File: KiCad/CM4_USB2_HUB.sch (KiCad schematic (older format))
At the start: 31 parts, among them IC1 USB2517-JZX, J10 72309-8014BLF, J11 10104110-0001LF, J12 SS-52100-002, J4 72309-8014BLF, J9 Conn_02x05_Odd_Even, U3 FSUSB42MUX, Y1 24MHz

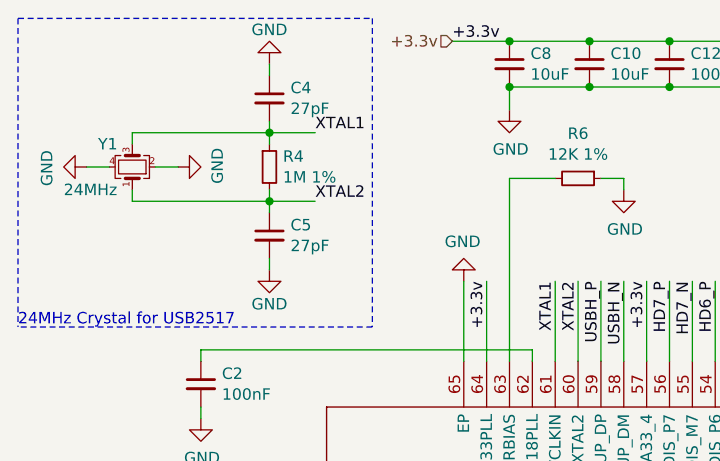
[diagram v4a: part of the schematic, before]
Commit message: Updated Y1 capacitors
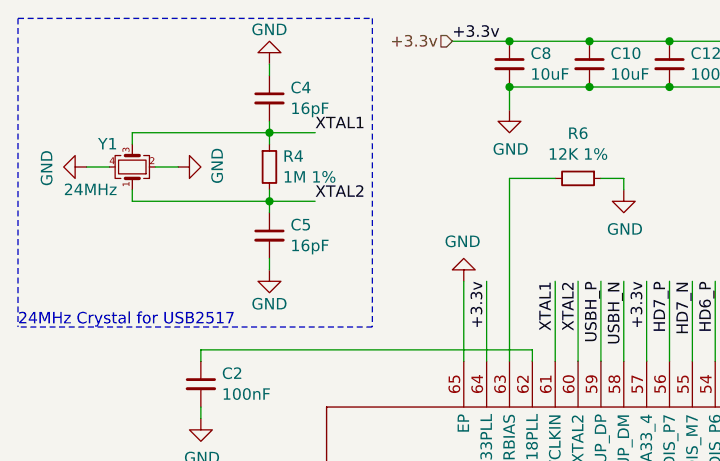
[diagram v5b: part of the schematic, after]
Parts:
- C4, C5: value 27pF -> 16pF; footprint (none) -> CM4_MATX:C_0402_1005Metric_Pad0.74x0.62mm_HandSolder; Description Load Capacitors for Y1 Crystal -> 10V 16pF X8R 0402 5% Tol; Mfr. (none) -> KEMET; Mfr. No (none) -> C0402C160J8HACTU; Mouser Part Number (none) -> 80-C0402C160J8HACTU; Mouser Price/Stock (none) -> https://www.mouser.co.uk/ProductDetail/KEMET/C0402C160J8HAC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
- R12: footprint (none) -> CM4_MATX:R_0603_1608Metric_Pad0.98x0.95mm_HandSolder
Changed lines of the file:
@@
 F 0 "R12" H 7850 6050 50  0000 L CNN
 F 1 "2.2K 1%" H 7700 5950 50  0000 L CNN
-F 2 "" H 8050 6000 50  0001 C CNN
+F 2 "CM4_MATX:R_0603_1608Metric_Pad0.98x0.95mm_HandSolder" H 8050 6000 50  0001 C CNN
 F 3 "~" H 8050 6000 50  0001 C CNN
 	1    8050 6000
@@
 P 1600 1450
 F 0 "C5" H 1692 1496 50  0000 L CNN
-F 1 "27pF" H 1692 1405 50  0000 L CNN
-F 2 "" H 1600 1450 50  0001 C CNN
-F 3 "~" H 1600 1450 50  0001 C CNN
-F 4 "Load Capacitors for Y1 Crystal" H 1600 1450 50  0001 C CNN "Description"
+F 1 "16pF" H 1692 1405 50  0000 L CNN
+F 2 "CM4_MATX:C_0402_1005Metric_Pad0.74x0.62mm_HandSolder" H 1600 1450 50  0001 C CNN
+F 3 "https://www.mouser.co.uk/datasheet/2/212/KEM_C1007_X8R_ULTRA_150C_SMD-1102703.pdf" H 1600 1450 50  0001 C CNN
+F 4 "10V 16pF X8R 0402 5% Tol" H 1600 1450 50  0001 C CNN "Description"
+F 5 "KEMET" H 1600 1450 50  0001 C CNN "Mfr."
+F 6 "C0402C160J8HACTU" H 1600 1450 50  0001 C CNN "Mfr. No"
+F 7 "80-C0402C160J8HACTU" H 1600 1450 50  0001 C CNN "Mouser Part Number"
+F 8 "https://www.mouser.co.uk/ProductDetail/KEMET/C0402C160J8HACTU/?qs=sGAEpiMZZMvsSlwiRhF8qtsBU8Zhqm2Rf2RCdR0OYjobkxwyt1Kljg%3D%3D" H 1600 1450 50  0001 C CNN "Mouser Price/Stock"
 	1    1600 1450
 	1    0    0    -1
@@
 P 1600 850
 F 0 "C4" H 1692 896 50  0000 L CNN
-F 1 "27pF" H 1692 805 50  0000 L CNN
-F 2 "" H 1600 850 50  0001 C CNN
-F 3 "~" H 1600 850 50  0001 C CNN
-F 4 "Load Capacitors for Y1 Crystal" H 1600 850 50  0001 C CNN "Description"
+F 1 "16pF" H 1692 805 50  0000 L CNN
+F 2 "CM4_MATX:C_0402_1005Metric_Pad0.74x0.62mm_HandSolder" H 1600 850 50  0001 C CNN
+F 3 "https://www.mouser.co.uk/datasheet/2/212/KEM_C1007_X8R_ULTRA_150C_SMD-1102703.pdf" H 1600 850 50  0001 C CNN
+F 4 "10V 16pF X8R 0402 5% Tol" H 1600 850 50  0001 C CNN "Description"
+F 5 "KEMET" H 1600 850 50  0001 C CNN "Mfr."
+F 6 "C0402C160J8HACTU" H 1600 850 50  0001 C CNN "Mfr. No"
+F 7 "80-C0402C160J8HACTU" H 1600 850 50  0001 C CNN "Mouser Part Number"
+F 8 "https://www.mouser.co.uk/ProductDetail/KEMET/C0402C160J8HACTU/?qs=sGAEpiMZZMvsSlwiRhF8qtsBU8Zhqm2Rf2RCdR0OYjobkxwyt1Kljg%3D%3D" H 1600 850 50  0001 C CNN "Mouser Price/Stock"
 	1    1600 850
 	1    0    0    -1

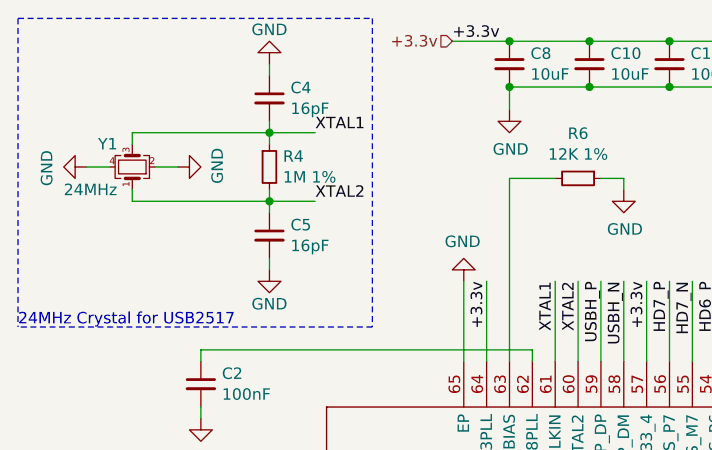
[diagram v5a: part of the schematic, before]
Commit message: Removed R4
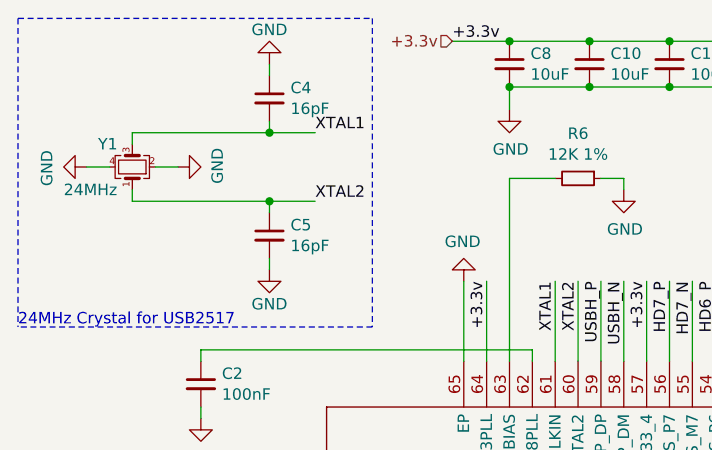
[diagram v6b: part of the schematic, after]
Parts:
- removed R4: 1M 1%, symbol CM4_MATX:R_Small
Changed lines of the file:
@@
 Wire Wire Line
 	1600 1000 1000 1000
-Wire Wire Line
-	1600 1300 1600 1250
 Connection ~ 1600 1300
 Wire Wire Line
@@
 Wire Wire Line
 	1600 1000 1800 1000
-Wire Wire Line
-	1600 1050 1600 1000
 $Comp
 L CM4_MATX:C_Small C5
@@
 Text Label 1800 1000 0    50   ~ 0
 XTAL1
-$Comp
-L CM4_MATX:R_Small R4
-U 1 1 5FE3FBDB
-P 1600 1150
-F 0 "R4" H 1659 1196 50  0000 L CNN
-F 1 "1M 1%" H 1659 1105 50  0000 L CNN
-F 2 "" H 1600 1150 50  0001 C CNN
-F 3 "~" H 1600 1150 50  0001 C CNN
-	1    1600 1150
-	1    0    0    -1
-$EndComp
 Wire Wire Line
 	900  1150 800  1150

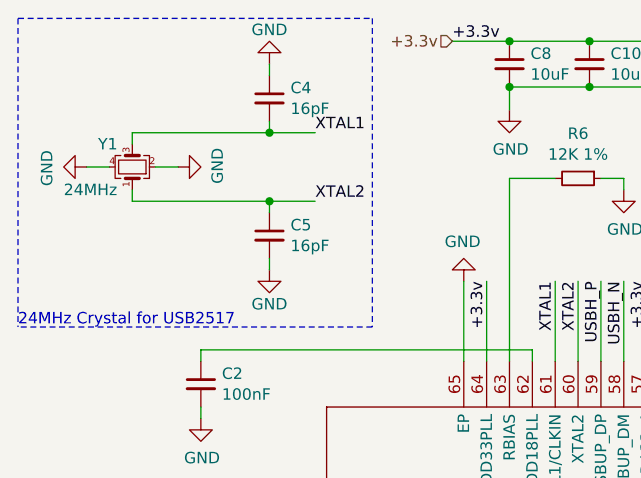
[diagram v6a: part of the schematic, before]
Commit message: Moved C4 and C5 in the schematic to be more logical
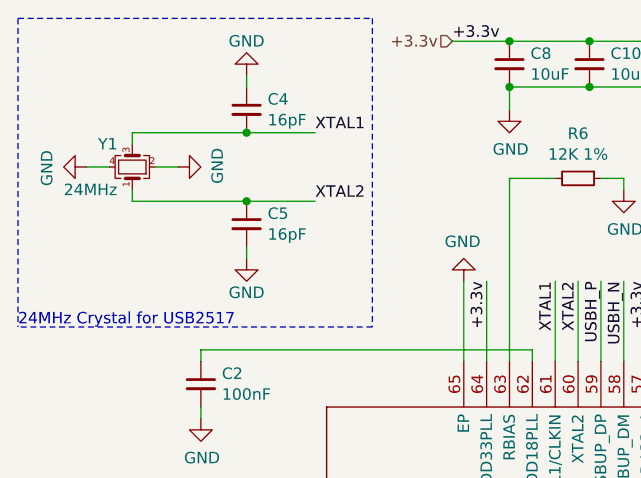
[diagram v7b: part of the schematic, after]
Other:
- moved on the sheet: C4, C5
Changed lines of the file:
@@
 	2650 1200 2650 2000
 Wire Wire Line
-	1000 1300 1600 1300
-Wire Wire Line
 	1000 1250 1000 1300
 Wire Wire Line
 	1000 1000 1000 1050
-Wire Wire Line
-	1600 1000 1000 1000
-Connection ~ 1600 1300
-Wire Wire Line
-	1600 1300 1800 1300
-Wire Wire Line
-	1600 1350 1600 1300
-Wire Wire Line
-	1600 1000 1600 950
-Connection ~ 1600 1000
-Wire Wire Line
-	1600 1000 1800 1000
 $Comp
 L CM4_MATX:C_Small C5
 U 1 1 5FE4748F
-P 1600 1450
-F 0 "C5" H 1692 1496 50  0000 L CNN
-F 1 "16pF" H 1692 1405 50  0000 L CNN
-F 2 "CM4_MATX:C_0402_1005Metric_Pad0.74x0.62mm_HandSolder" H 1600 1450 50  0001 C CNN
-F 3 "https://www.mouser.co.uk/datasheet/2/212/KEM_C1007_X8R_ULTRA_150C_SMD-1102703.pdf" H 1600 1450 50  0001 C CNN
-F 4 "10V 16pF X8R 0402 5% Tol" H 1600 1450 50  0001 C CNN "Description"
-F 5 "KEMET" H 1600 1450 50  0001 C CNN "Mfr."
-F 6 "C0402C160J8HACTU" H 1600 1450 50  0001 C CNN "Mfr. No"
-F 7 "80-C0402C160J8HACTU" H 1600 1450 50  0001 C CNN "Mouser Part Number"
-F 8 "https://www.mouser.co.uk/ProductDetail/KEMET/C0402C160J8HACTU/?qs=sGAEpiMZZMvsSlwiRhF8qtsBU8Zhqm2Rf2RCdR0OYjobkxwyt1Kljg%3D%3D" H 1600 1450 50  0001 C CNN "Mouser Price/Stock"
-	1    1600 1450
+P 1500 1400
+F 0 "C5" H 1592 1446 50  0000 L CNN
+F 1 "16pF" H 1592 1355 50  0000 L CNN
+F 2 "CM4_MATX:C_0402_1005Metric_Pad0.74x0.62mm_HandSolder" H 1500 1400 50  0001 C CNN
+F 3 "https://www.mouser.co.uk/datasheet/2/212/KEM_C1007_X8R_ULTRA_150C_SMD-1102703.pdf" H 1500 1400 50  0001 C CNN
+F 4 "10V 16pF X8R 0402 5% Tol" H 1500 1400 50  0001 C CNN "Description"
+F 5 "KEMET" H 1500 1400 50  0001 C CNN "Mfr."
+F 6 "C0402C160J8HACTU" H 1500 1400 50  0001 C CNN "Mfr. No"
+F 7 "80-C0402C160J8HACTU" H 1500 1400 50  0001 C CNN "Mouser Part Number"
+F 8 "https://www.mouser.co.uk/ProductDetail/KEMET/C0402C160J8HACTU/?qs=sGAEpiMZZMvsSlwiRhF8qtsBU8Zhqm2Rf2RCdR0OYjobkxwyt1Kljg%3D%3D" H 1500 1400 50  0001 C CNN "Mouser Price/Stock"
+	1    1500 1400
 	1    0    0    -1
 $EndComp
@@
 L CM4_MATX:C_Small C4
 U 1 1 5FE47231
-P 1600 850
-F 0 "C4" H 1692 896 50  0000 L CNN
-F 1 "16pF" H 1692 805 50  0000 L CNN
-F 2 "CM4_MATX:C_0402_1005Metric_Pad0.74x0.62mm_HandSolder" H 1600 850 50  0001 C CNN
-F 3 "https://www.mouser.co.uk/datasheet/2/212/KEM_C1007_X8R_ULTRA_150C_SMD-1102703.pdf" H 1600 850 50  0001 C CNN
-F 4 "10V 16pF X8R 0402 5% Tol" H 1600 850 50  0001 C CNN "Description"
-F 5 "KEMET" H 1600 850 50  0001 C CNN "Mfr."
-F 6 "C0402C160J8HACTU" H 1600 850 50  0001 C CNN "Mfr. No"
-F 7 "80-C0402C160J8HACTU" H 1600 850 50  0001 C CNN "Mouser Part Number"
-F 8 "https://www.mouser.co.uk/ProductDetail/KEMET/C0402C160J8HACTU/?qs=sGAEpiMZZMvsSlwiRhF8qtsBU8Zhqm2Rf2RCdR0OYjobkxwyt1Kljg%3D%3D" H 1600 850 50  0001 C CNN "Mouser Price/Stock"
-	1    1600 850
+P 1500 900
+F 0 "C4" H 1592 946 50  0000 L CNN
+F 1 "16pF" H 1592 855 50  0000 L CNN
+F 2 "CM4_MATX:C_0402_1005Metric_Pad0.74x0.62mm_HandSolder" H 1500 900 50  0001 C CNN
+F 3 "https://www.mouser.co.uk/datasheet/2/212/KEM_C1007_X8R_ULTRA_150C_SMD-1102703.pdf" H 1500 900 50  0001 C CNN
+F 4 "10V 16pF X8R 0402 5% Tol" H 1500 900 50  0001 C CNN "Description"
+F 5 "KEMET" H 1500 900 50  0001 C CNN "Mfr."
+F 6 "C0402C160J8HACTU" H 1500 900 50  0001 C CNN "Mfr. No"
+F 7 "80-C0402C160J8HACTU" H 1500 900 50  0001 C CNN "Mouser Part Number"
+F 8 "https://www.mouser.co.uk/ProductDetail/KEMET/C0402C160J8HACTU/?qs=sGAEpiMZZMvsSlwiRhF8qtsBU8Zhqm2Rf2RCdR0OYjobkxwyt1Kljg%3D%3D" H 1500 900 50  0001 C CNN "Mouser Price/Stock"
+	1    1500 900
 	1    0    0    -1
 $EndComp
@@
 L CM4_MATX:GND #PWR0133
 U 1 1 5FCE87B8
-P 1600 1600
-F 0 "#PWR0133" H 1600 1350 50  0001 C CNN
-F 1 "GND" H 1600 1450 50  0000 C CNN
-F 2 "" H 1600 1600 50  0001 C CNN
-F 3 "" H 1600 1600 50  0001 C CNN
-	1    1600 1600
-	1    0    0    -1
-$EndComp
-Wire Wire Line
-	1600 1550 1600 1600
+P 1500 1550
+F 0 "#PWR0133" H 1500 1300 50  0001 C CNN
+F 1 "GND" H 1500 1400 50  0000 C CNN
+F 2 "" H 1500 1550 50  0001 C CNN
+F 3 "" H 1500 1550 50  0001 C CNN
+	1    1500 1550
+	1    0    0    -1
+$EndComp
+Wire Wire Line
+	1500 1500 1500 1550
 $Comp
 L CM4_MATX:GND #PWR0134
 U 1 1 5FCF3652
-P 1600 700
-F 0 "#PWR0134" H 1600 450 50  0001 C CNN
-F 1 "GND" H 1600 550 50  0000 C CNN
-F 2 "" H 1600 700 50  0001 C CNN
-F 3 "" H 1600 700 50  0001 C CNN
-	1    1600 700
+P 1500 750
+F 0 "#PWR0134" H 1500 500 50  0001 C CNN
+F 1 "GND" H 1500 600 50  0000 C CNN
+F 2 "" H 1500 750 50  0001 C CNN
+F 3 "" H 1500 750 50  0001 C CNN
+	1    1500 750
 	-1   0    0    1
 $EndComp
 Wire Wire Line
-	1600 750  1600 700
+	1500 800  1500 750
 Wire Notes Line
 	2050 1850 500  1850
@@
 	1    0    0    -1
 $EndComp
+Wire Wire Line
+	1000 1300 1500 1300
+Wire Wire Line
+	1000 1000 1500 1000
+Connection ~ 1500 1000
+Wire Wire Line
+	1500 1000 1800 1000
+Connection ~ 1500 1300
+Wire Wire Line
+	1500 1300 1800 1300
 $EndSCHEMATC
